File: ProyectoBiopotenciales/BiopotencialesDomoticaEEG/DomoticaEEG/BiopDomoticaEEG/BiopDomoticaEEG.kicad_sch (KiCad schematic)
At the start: 11 parts

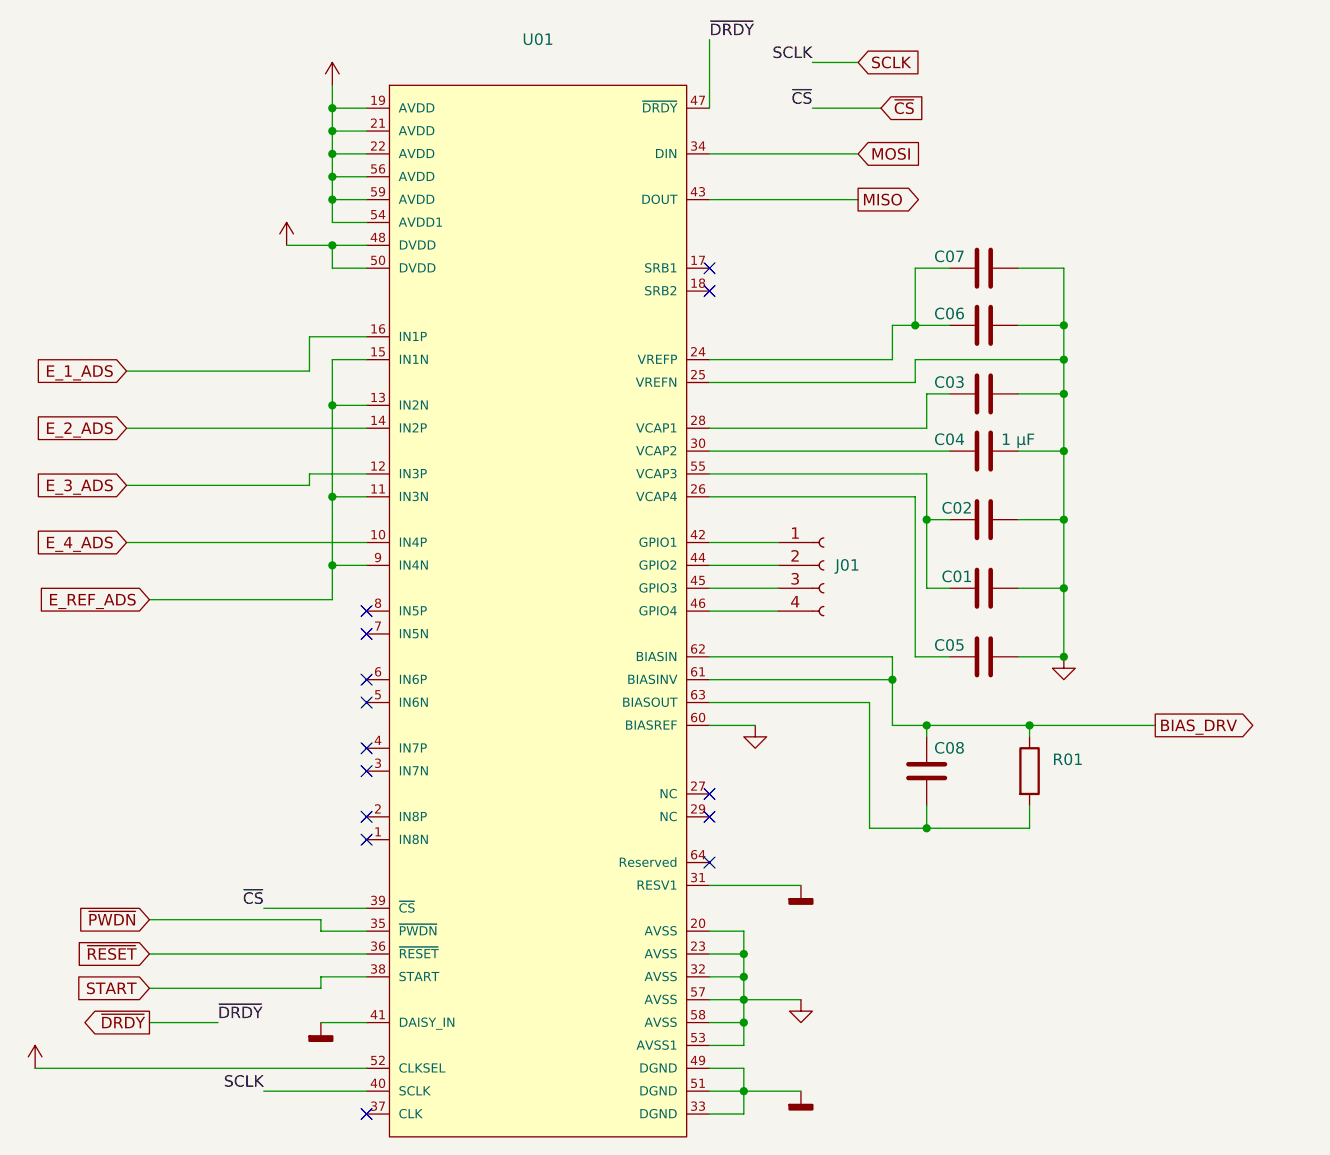
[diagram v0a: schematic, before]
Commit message: feat: first aproach of schematic finished
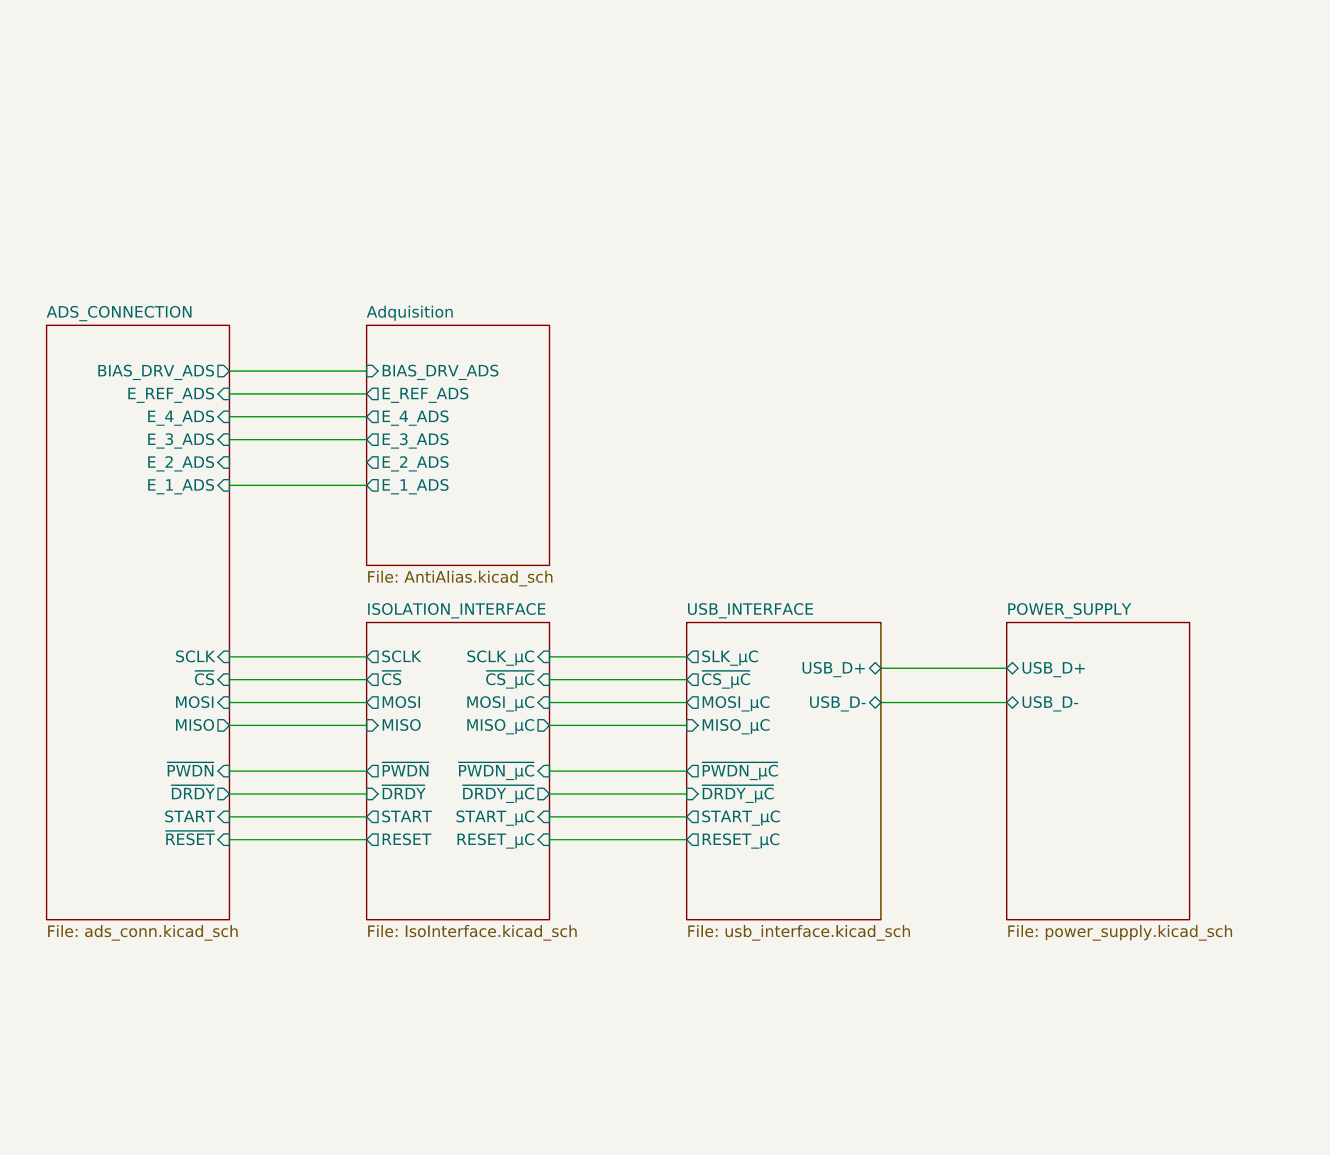
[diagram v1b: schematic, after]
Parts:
- removed C01, C02: (no value), symbol Device:C
- removed C03, C05, C06, C07, C08: (no value), Capacitor_SMD:C_0201_0603Metric_Pad0.64x0.40mm_HandSolder, symbol Device:C
- removed C04: 1 µF, Capacitor_SMD:C_0201_0603Metric_Pad0.64x0.40mm_HandSolder, symbol Device:C
- removed J01: (no value), symbol Connector:Conn_01x04_Female
- removed R01: (no value), symbol Device:R
- removed U01: (no value), symbol eec:ADS1299-4PAGR
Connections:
- no-connect marks 14 -> 0
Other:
- added sheet ADS_CONNECTION (ads_conn.kicad_sch)
- added sheet Adquisition (AntiAlias.kicad_sch)
- added sheet ISOLATION_INTERFACE (IsoInterface.kicad_sch)
- added sheet POWER_SUPPLY (power_supply.kicad_sch)
- added sheet USB_INTERFACE (usb_interface.kicad_sch)

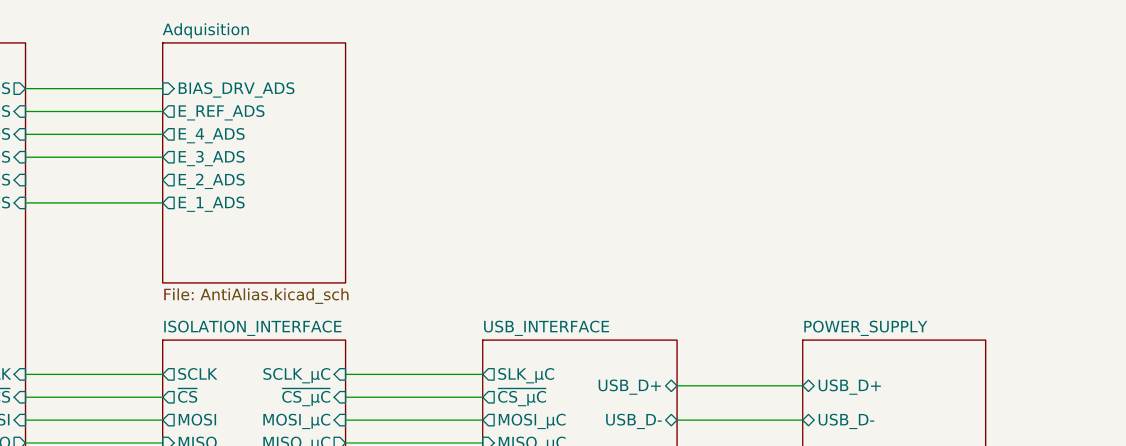
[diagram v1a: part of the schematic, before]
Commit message: feat: more info for block diagram
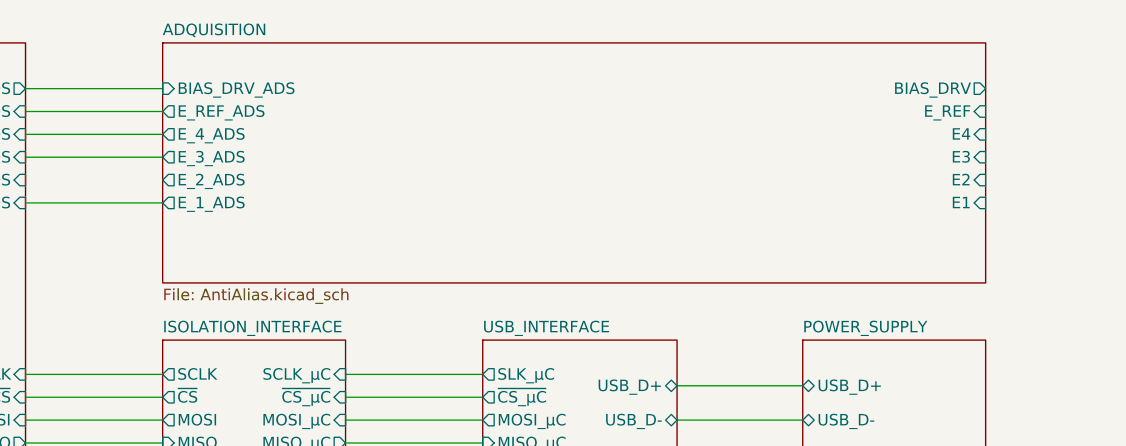
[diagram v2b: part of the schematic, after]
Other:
- sheet Adquisition renamed ADQUISITION
- sheet ADQUISITION ports: added BIAS_DRV, E1, E2, E3, E4, E_REF; removed none
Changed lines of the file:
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@@
     )
   )
-  (sheet (at 118.11 66.04) (size 20.32 26.67) (fields_autoplaced)
+  (sheet (at 118.11 66.04) (size 91.44 26.67) (fields_autoplaced)
     (stroke (width 0.1524) (type solid) (color 0 0 0 0))
     (fill (color 0 0 0 0.0000))
-    (property "Sheet name" "Adquisition" (id 0) (at 118.11 65.3284 0)
+    (property "Sheet name" "ADQUISITION" (id 0) (at 118.11 65.3284 0)
       (effects (font (size 1.27 1.27)) (justify left bottom))
     )
@@
       (effects (font (size 1.27 1.27)) (justify left))
     )
+    (pin "E3" input (at 209.55 78.74 0)
+      (effects (font (size 1.27 1.27)) (justify right))
+    )
+    (pin "E1" input (at 209.55 83.82 0)
+      (effects (font (size 1.27 1.27)) (justify right))
+    )
+    (pin "E2" input (at 209.55 81.28 0)
+      (effects (font (size 1.27 1.27)) (justify right))
+    )
+    (pin "BIAS_DRV" output (at 209.55 71.12 0)
+      (effects (font (size 1.27 1.27)) (justify right))
+    )
+    (pin "E_REF" input (at 209.55 73.66 0)
+      (effects (font (size 1.27 1.27)) (justify right))
+    )
+    (pin "E4" input (at 209.55 76.2 0)
+      (effects (font (size 1.27 1.27)) (justify right))
+    )
   )
